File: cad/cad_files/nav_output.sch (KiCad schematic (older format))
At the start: 7 parts

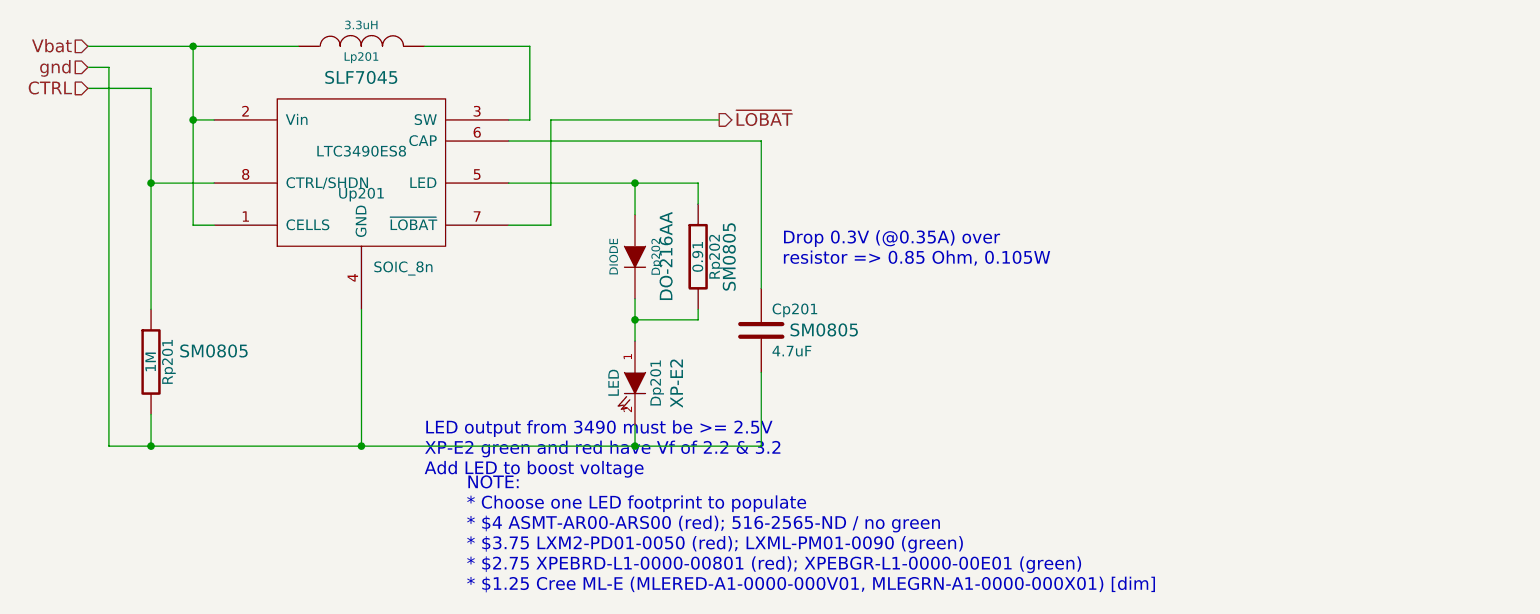
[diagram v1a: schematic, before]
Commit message: Prep for layout (continued)
add footprints, refine design
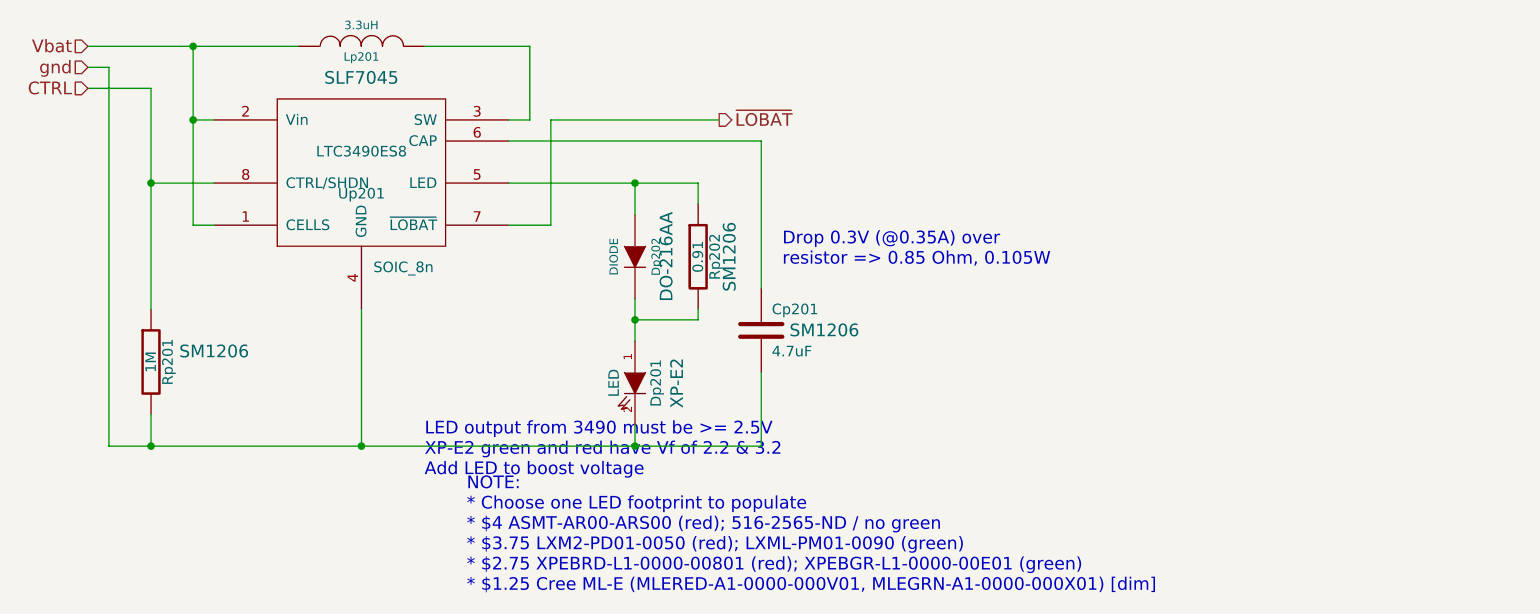
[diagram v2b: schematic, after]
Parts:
- Cp201, Rp201, Rp202: footprint SM0805 -> SM1206
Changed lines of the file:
@@
-EESchema Schematic File Version 2  date Wed 10 Dec 2014 07:12:18 PM HST
+EESchema Schematic File Version 2  date Thu 11 Dec 2014 12:57:18 AM HST
 LIBS:local_parts
 LIBS:power
@@
 F 0 "Rp202" V 6680 4400 50  0000 C CNN
 F 1 "0.91" V 6600 4400 50  0000 C CNN
-F 2 "SM0805" V 6750 4400 60  0000 C CNN
+F 2 "SM1206" V 6750 4400 60  0000 C CNN
 F 4 "CRM0805-FX-R910ELF" V 6600 4400 60  0001 C CNN "digikey"
 	1    6600 4400
@@
 F 0 "Cp201" H 6950 4850 50  0000 L CNN
 F 1 "4.7uF" H 6950 4650 50  0000 L CNN
-F 2 "SM0805" H 7200 4750 60  0000 C CNN
+F 2 "SM1206" H 7200 4750 60  0000 C CNN
 F 4 "445-1421-1-ND" H 6900 4750 60  0001 C CNN "digikey"
 	1    6900 4750
@@
 F 0 "Rp201" V 4080 4900 50  0000 C CNN
 F 1 "1M" V 4000 4900 50  0000 C CNN
-F 2 "SM0805" H 4300 4950 60  0000 C CNN
+F 2 "SM1206" H 4300 4950 60  0000 C CNN
 F 4 "P1.00MCCT-ND" V 4000 4900 60  0001 C CNN "digikey"
 	1    4000 4900

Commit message: Prep for layout (continued)
Add footprints, refine design

add additional ``LED footprint'' (pin header)
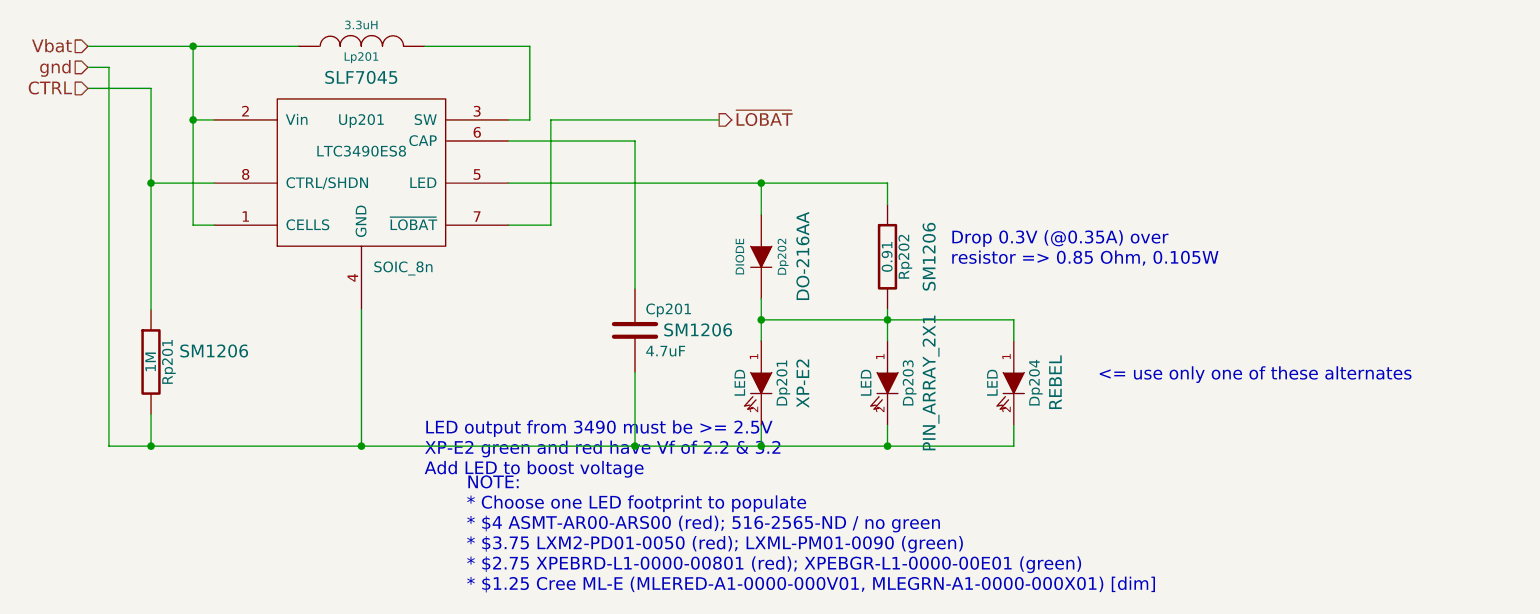
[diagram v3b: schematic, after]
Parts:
- added Dp203: LED, PIN_ARRAY_2X1, symbol LED
- added Dp204: LED, REBEL, symbol LED
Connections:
- net gnd: now also Dp203.2 (K), Dp204.2 (K)
- net at Dp201.1 (A), Dp202.2 (K), Rp202.2: now also Dp203.1 (A), Dp204.1 (A)
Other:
- note added: "<= use only one of these alternates"
- moved on the sheet: Cp201, Dp201, Dp202, Rp202
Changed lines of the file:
@@
-EESchema Schematic File Version 2  date Thu 11 Dec 2014 12:57:18 AM HST
+EESchema Schematic File Version 2  date Thu 11 Dec 2014 02:09:55 AM HST
 LIBS:local_parts
 LIBS:power
@@
 Comment4 ""
 $EndDescr
-Text Notes 7000 4450 0    60   ~ 0
+Text Notes 8500 5000 0    60   ~ 0
+<= use only one of these alternates
+Wire Wire Line
+	8100 4800 8100 4700
+Wire Wire Line
+	8100 4700 6900 4700
+Connection ~ 6900 5300
+Wire Wire Line
+	7500 5300 7500 5200
+Connection ~ 6900 4700
+Wire Wire Line
+	7500 4650 7500 4800
+Wire Wire Line
+	5000 5300 5000 4650
+Wire Wire Line
+	6900 4200 6900 4050
+Connection ~ 4000 4050
+Wire Wire Line
+	4000 4650 4000 3600
+Connection ~ 4000 5300
+Wire Wire Line
+	3800 3500 3800 5300
+Wire Wire Line
+	3800 3500 3700 3500
+Connection ~ 6300 5300
+Wire Wire Line
+	6300 4950 6300 5300
+Wire Wire Line
+	4000 5300 4000 5150
+Wire Wire Line
+	6300 4550 6300 3850
+Wire Wire Line
+	6300 3850 5700 3850
+Connection ~ 4200 3750
+Wire Wire Line
+	4200 3400 4200 4250
+Wire Wire Line
+	4300 3750 4200 3750
+Wire Wire Line
+	4200 4250 4300 4250
+Wire Wire Line
+	4300 4050 4000 4050
+Wire Wire Line
+	5300 3400 5800 3400
+Wire Wire Line
+	5800 3400 5800 3750
+Wire Wire Line
+	5800 3750 5700 3750
+Wire Wire Line
+	6900 5300 6900 5200
+Connection ~ 5000 5300
+Wire Wire Line
+	3700 3400 4700 3400
+Connection ~ 4200 3400
+Wire Wire Line
+	4000 3600 3700 3600
+Wire Wire Line
+	6700 3750 5900 3750
+Wire Wire Line
+	5900 3750 5900 4250
+Wire Wire Line
+	5900 4250 5700 4250
+Wire Wire Line
+	6900 4600 6900 4800
+Wire Wire Line
+	5700 4050 7500 4050
+Wire Wire Line
+	7500 4050 7500 4150
+Connection ~ 6900 4050
+Connection ~ 7500 4700
+Wire Wire Line
+	8100 5200 8100 5300
+Wire Wire Line
+	8100 5300 3800 5300
+Connection ~ 7500 5300
+$Comp
+L LED Dp204
+U 1 1 54897A04
+P 8100 5000
+F 0 "Dp204" H 8100 5100 50  0000 C CNN
+F 1 "LED" H 8100 4900 50  0000 C CNN
+F 2 "REBEL" H 8100 5200 60  0000 C CNN
+F 4 "XPEBRD-L1-0000-00801CT-ND" H 8100 5000 60  0001 C CNN "digikey"
+	1    8100 5000
+	0    1    1    0
+$EndComp
+$Comp
+L LED Dp203
+U 1 1 54897986
+P 7500 5000
+F 0 "Dp203" H 7500 5100 50  0000 C CNN
+F 1 "LED" H 7500 4900 50  0000 C CNN
+F 2 "PIN_ARRAY_2X1" H 7500 5200 60  0000 C CNN
+F 4 "XPEBRD-L1-0000-00801CT-ND" H 7500 5000 60  0001 C CNN "digikey"
+	1    7500 5000
+	0    1    1    0
+$EndComp
+Text Notes 7800 4450 0    60   ~ 0
 Drop 0.3V (@0.35A) over \nresistor => 0.85 Ohm, 0.105W
-Connection ~ 6300 4050
-Wire Wire Line
-	6600 4050 6600 4150
-Wire Wire Line
-	5700 4050 6600 4050
-Wire Wire Line
-	6300 4600 6300 4800
-Wire Wire Line
-	5700 4250 5900 4250
-Wire Wire Line
-	5900 4250 5900 3750
-Wire Wire Line
-	5900 3750 6700 3750
-Wire Wire Line
-	4000 3600 3700 3600
-Connection ~ 4200 3400
-Wire Wire Line
-	3700 3400 4700 3400
-Connection ~ 5000 5300
-Wire Wire Line
-	6300 5200 6300 5300
-Wire Wire Line
-	5700 3750 5800 3750
-Wire Wire Line
-	5800 3750 5800 3400
-Wire Wire Line
-	5800 3400 5300 3400
-Wire Wire Line
-	4300 4050 4000 4050
-Wire Wire Line
-	4200 4250 4300 4250
-Wire Wire Line
-	4300 3750 4200 3750
-Wire Wire Line
-	4200 3400 4200 4250
-Connection ~ 4200 3750
-Wire Wire Line
-	5700 3850 6900 3850
-Wire Wire Line
-	6900 3850 6900 4550
-Wire Wire Line
-	4000 5300 4000 5150
-Wire Wire Line
-	6900 5300 6900 4950
-Wire Wire Line
-	6900 5300 3800 5300
-Connection ~ 6300 5300
-Wire Wire Line
-	3700 3500 3800 3500
-Wire Wire Line
-	3800 3500 3800 5300
-Connection ~ 4000 5300
-Wire Wire Line
-	4000 4650 4000 3600
-Connection ~ 4000 4050
-Wire Wire Line
-	6300 4050 6300 4200
-Wire Wire Line
-	5000 5300 5000 4650
-Wire Wire Line
-	6300 4700 6600 4700
-Wire Wire Line
-	6600 4700 6600 4650
-Connection ~ 6300 4700
 $Comp
 L R Rp202
 U 1 1 54813C92
-P 6600 4400
-F 0 "Rp202" V 6680 4400 50  0000 C CNN
-F 1 "0.91" V 6600 4400 50  0000 C CNN
-F 2 "SM1206" V 6750 4400 60  0000 C CNN
-F 4 "CRM0805-FX-R910ELF" V 6600 4400 60  0001 C CNN "digikey"
-	1    6600 4400
+P 7500 4400
+F 0 "Rp202" V 7580 4400 50  0000 C CNN
+F 1 "0.91" V 7500 4400 50  0000 C CNN
+F 2 "SM1206" V 7700 4400 60  0000 C CNN
+F 4 "CRM0805-FX-R910ELF" V 7500 4400 60  0001 C CNN "digikey"
+	1    7500 4400
 	1    0    0    -1
 $EndComp
@@
 L DIODE Dp202
 U 1 1 548139A3
-P 6300 4400
-F 0 "Dp202" H 6300 4500 40  0000 C CNN
-F 1 "DIODE" H 6300 4300 40  0000 C CNN
-F 2 "DO-216AA" H 6300 4550 60  0000 C CNN
-F 4 "MBRM120ET3GOSCT-ND" H 6300 4400 60  0001 C CNN "digikey"
-	1    6300 4400
+P 6900 4400
+F 0 "Dp202" H 6900 4500 40  0000 C CNN
+F 1 "DIODE" H 6900 4300 40  0000 C CNN
+F 2 "DO-216AA" H 6900 4600 60  0000 C CNN
+F 4 "MBRM120ET3GOSCT-ND" H 6900 4400 60  0001 C CNN "digikey"
+	1    6900 4400
 	0    1    1    0
 $EndComp
@@
 L LED Dp201
 U 1 1 53D0E361
-P 6300 5000
-F 0 "Dp201" H 6300 5100 50  0000 C CNN
-F 1 "LED" H 6300 4900 50  0000 C CNN
-F 2 "XP-E2" H 6300 5200 60  0000 C CNN
-F 4 "XPEBRD-L1-0000-00801CT-ND" H 6300 5000 60  0001 C CNN "digikey"
-	1    6300 5000
+P 6900 5000
+F 0 "Dp201" H 6900 5100 50  0000 C CNN
+F 1 "LED" H 6900 4900 50  0000 C CNN
+F 2 "XP-E2" H 6900 5200 60  0000 C CNN
+F 4 "XPEBRD-L1-0000-00801CT-ND" H 6900 5000 60  0001 C CNN "digikey"
+	1    6900 5000
 	0    1    1    0
 $EndComp
@@
 L C Cp201
 U 1 1 53D0E16B
-P 6900 4750
-F 0 "Cp201" H 6950 4850 50  0000 L CNN
-F 1 "4.7uF" H 6950 4650 50  0000 L CNN
-F 2 "SM1206" H 7200 4750 60  0000 C CNN
-F 4 "445-1421-1-ND" H 6900 4750 60  0001 C CNN "digikey"
-	1    6900 4750
+P 6300 4750
+F 0 "Cp201" H 6350 4850 50  0000 L CNN
+F 1 "4.7uF" H 6350 4650 50  0000 L CNN
+F 2 "SM1206" H 6600 4750 60  0000 C CNN
+F 4 "445-1421-1-ND" H 6300 4750 60  0001 C CNN "digikey"
+	1    6300 4750
 	1    0    0    -1
 $EndComp
@@
 U 1 1 53D0DE6A
 P 5000 4000
-F 0 "Up201" H 5000 3900 50  0000 C CNN
+F 0 "Up201" H 5000 4250 50  0000 C CNN
 F 1 "LTC3490ES8" H 5000 4100 50  0000 C CNN
 F 2 "SOIC_8n" H 5200 3550 50  0000 C CNN

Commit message: Updates during layout
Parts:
- Dp204: footprint REBEL -> LED-rebel_sketch
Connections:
- net p2_sw: now reaches Lp201.2, Up201.3 (SW)
- net p2_LED_out: now reaches Dp202.1 (A), Rp202.1, Up201.5 (LED)
- net p2_cap: now reaches Cp201.1, Up201.6 (CAP)
- net p2_LED_mid: now reaches Dp201.1 (A), Dp202.2 (K), Dp203.1 (A), Dp204.1 (A), Rp202.2
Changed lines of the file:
@@
-EESchema Schematic File Version 2  date Thu 11 Dec 2014 02:09:55 AM HST
+EESchema Schematic File Version 2  date Tue 16 Dec 2014 01:21:59 AM HST
 LIBS:local_parts
 LIBS:power
@@
 Sheet 4 4
 Title "LED Driver"
-Date "11 dec 2014"
+Date "16 dec 2014"
 Rev ""
 Comp ""
@@
 Comment4 ""
 $EndDescr
+Text Label 7900 4700 0    60   ~ 0
+p2_LED_mid
+Text Label 6400 4050 0    60   ~ 0
+p2_LED_out
+Text Label 6300 4400 1    60   ~ 0
+p2_cap
+Text Label 5500 3400 0    60   ~ 0
+p2_sw
 Text Notes 8500 5000 0    60   ~ 0
 <= use only one of these alternates
@@
 F 0 "Dp204" H 8100 5100 50  0000 C CNN
 F 1 "LED" H 8100 4900 50  0000 C CNN
-F 2 "REBEL" H 8100 5200 60  0000 C CNN
+F 2 "LED-rebel_sketch" H 8100 5200 60  0000 C CNN
 F 4 "XPEBRD-L1-0000-00801CT-ND" H 8100 5000 60  0001 C CNN "digikey"
 	1    8100 5000
